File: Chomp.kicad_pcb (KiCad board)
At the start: 2 copper layers, 138.1 x 47.6 mm, 32 parts, among them J1 IN2, J10 V2-5, J11 V2-8, J12 V2-6, J13 T2-B, J14 T2-G, J2 IN1, J3 V1-2, J4 V1-1, J5 V1-3, J6 RV1-1, J7 RV1-3, J8 V1-6, J9 V1-8

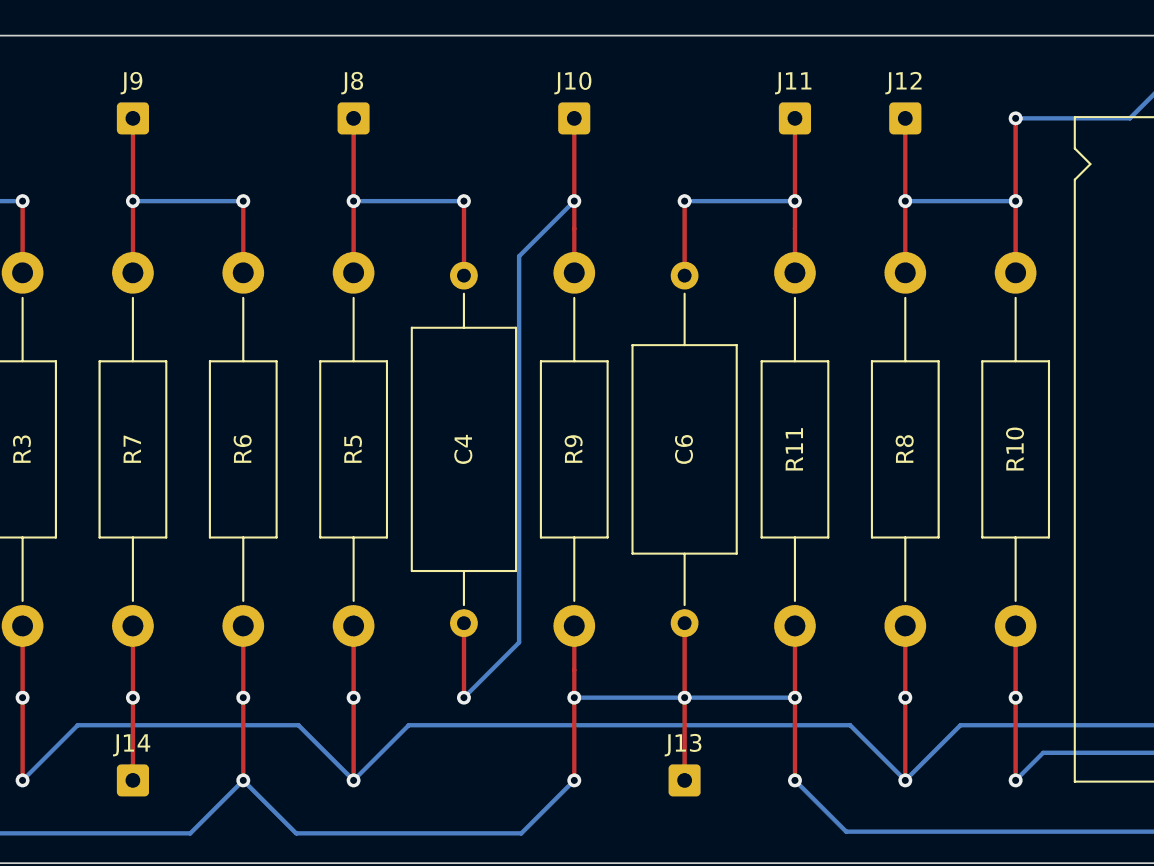
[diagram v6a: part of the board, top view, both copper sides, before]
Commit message: Convert to 5E1.
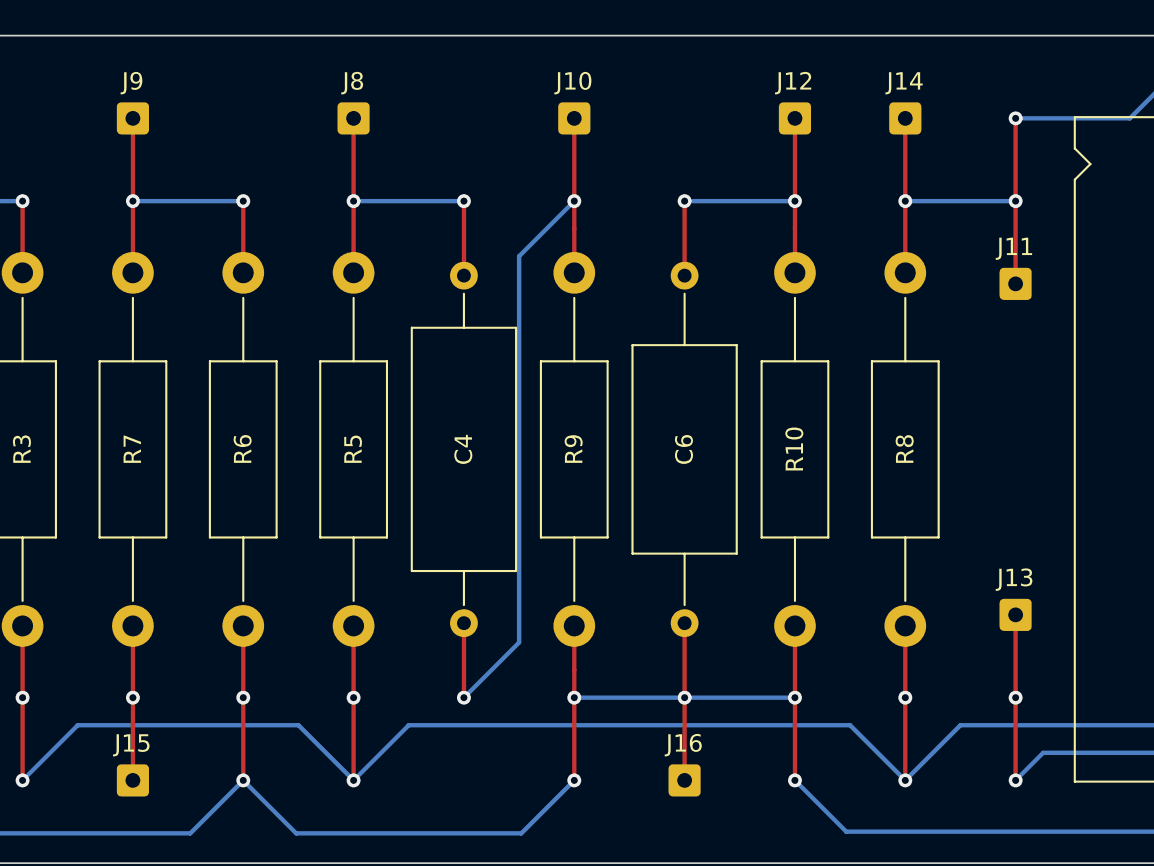
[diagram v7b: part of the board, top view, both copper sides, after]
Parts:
- removed the R10 at (171.4, 94.6)
- added J11: L1-1, Connector_Wire:SolderWire-0.25sqmm_1x01_D0.65mm_OD1.7mm, F.Cu at (171.4, 95.2)
- added J13: L1-2, Connector_Wire:SolderWire-0.25sqmm_1x01_D0.65mm_OD1.7mm, F.Cu at (171.4, 114.3)
- renumbered J11 to J12, J12 to J14, J14 to J15, J13 to J16, R11 to R10
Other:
- board text removed: "This is not a PCB layout, it's a wiring diagram for a U-Style turret strip (CED-P-HTBU-2X18). Traces should be populated as wire leads as needed."

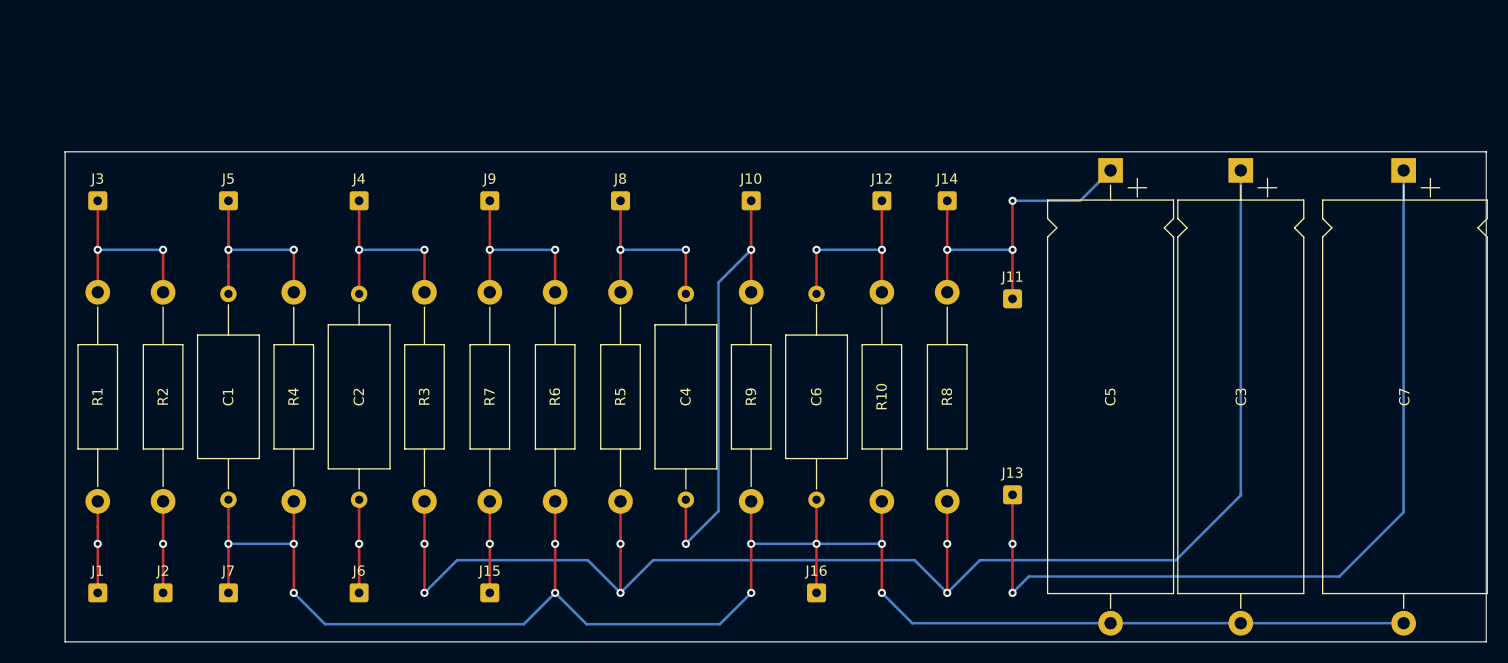
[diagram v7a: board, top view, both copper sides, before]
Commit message: Simplify choke wiring.
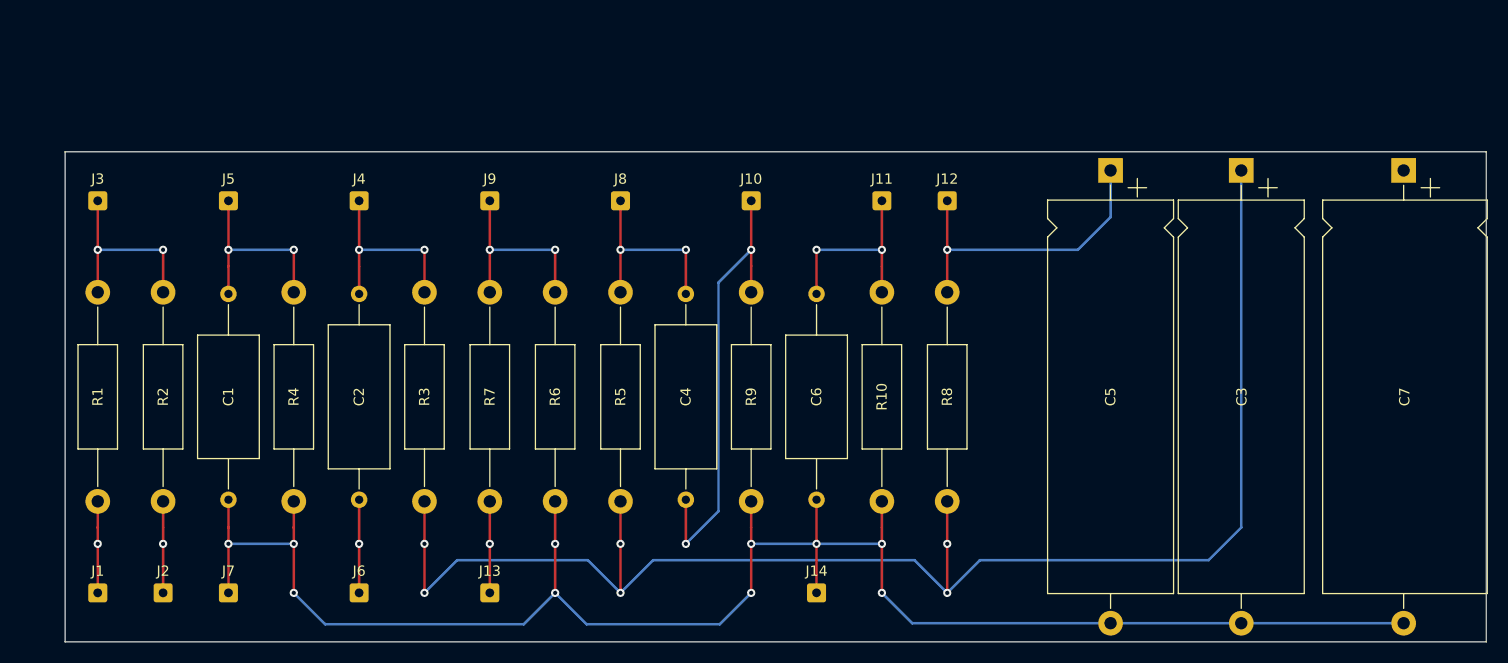
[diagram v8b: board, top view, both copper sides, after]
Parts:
- removed the J11 at (171.4, 95.2)
- removed the J13 at (171.4, 114.3)
- C3, C5: value 8 -> 10
- C7: value 16 -> 15
- renumbered J12 to J11, J14 to J12, J15 to J13, J16 to J14
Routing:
- net Net-(C7-Pad1): track 83.4 -> 0.00 mm, vias 2 -> 0
- net Net-(C5-Pad1): track 34.9 -> 30.6 mm, vias 3 -> 1
- net Net-(C3-Pad1): track 146.8 -> 148.6 mm
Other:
- board text removed: "15"
